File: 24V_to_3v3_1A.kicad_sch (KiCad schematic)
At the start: 6 parts, among them U2 R-78E3.3-1.0

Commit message: 24V updates
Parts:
- renumbered C12 to C3, C13 to C4, C14 to C5, C15 to C6, U2 to U1
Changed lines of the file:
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@@
   (symbol (lib_id "Regulator_Switching:R-78E3.3-1.0") (at 121.92 80.01 0) (unit 1)
     (in_bom yes) (on_board yes)
-    (property "Reference" "U2" (id 0) (at 121.92 73.8632 0))
+    (property "Reference" "U1" (id 0) (at 121.92 73.8632 0))
     (property "Value" "R-78E3.3-1.0" (id 1) (at 121.92 76.1746 0))
     (property "Footprint" "Converter_DCDC:Converter_DCDC_RECOM_R-78E-0.5_THT" (id 2) (at 123.19 86.36 0)
@@
   (symbol (lib_id "Device:C") (at 106.68 83.82 0) (unit 1)
     (in_bom yes) (on_board yes)
-    (property "Reference" "C13" (id 0) (at 109.601 82.6516 0)
+    (property "Reference" "C4" (id 0) (at 109.601 82.6516 0)
       (effects (font (size 1.27 1.27)) (justify left))
     )
@@
   (symbol (lib_id "Device:C") (at 96.52 83.82 0) (unit 1)
     (in_bom yes) (on_board yes)
-    (property "Reference" "C12" (id 0) (at 99.441 82.6516 0)
+    (property "Reference" "C3" (id 0) (at 99.441 82.6516 0)
       (effects (font (size 1.27 1.27)) (justify left))
     )
@@
   (symbol (lib_id "Device:C") (at 135.89 83.82 0) (unit 1)
     (in_bom yes) (on_board yes)
-    (property "Reference" "C14" (id 0) (at 138.811 82.6516 0)
+    (property "Reference" "C5" (id 0) (at 138.811 82.6516 0)
       (effects (font (size 1.27 1.27)) (justify left))
     )
@@
   (symbol (lib_id "Device:C") (at 148.59 83.82 0) (unit 1)
     (in_bom yes) (on_board yes)
-    (property "Reference" "C15" (id 0) (at 151.511 82.6516 0)
+    (property "Reference" "C6" (id 0) (at 151.511 82.6516 0)
       (effects (font (size 1.27 1.27)) (justify left))
     )
@@
   (symbol (lib_id "power:PWR_FLAG") (at 109.22 80.01 0) (unit 1)
     (in_bom yes) (on_board yes)
-    (property "Reference" "#FLG05" (id 0) (at 109.22 78.105 0)
+    (property "Reference" "#FLG04" (id 0) (at 109.22 78.105 0)
       (effects (font (size 1.27 1.27)) hide)
     )

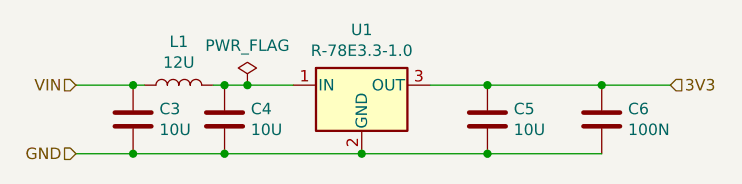
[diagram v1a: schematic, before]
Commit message: fix LT1161 symbol/sch
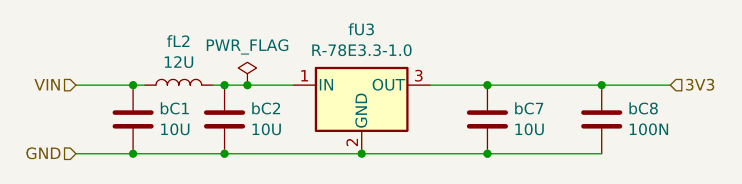
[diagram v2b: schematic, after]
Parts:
- renumbered C3 to bC1, C4 to bC2, C5 to bC7, C6 to bC8, L1 to fL2, U1 to fU3
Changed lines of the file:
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@@
   (symbol (lib_id "Regulator_Switching:R-78E3.3-1.0") (at 121.92 80.01 0) (unit 1)
     (in_bom yes) (on_board yes)
-    (property "Reference" "U1" (id 0) (at 121.92 73.8632 0))
+    (property "Reference" "fU3" (id 0) (at 121.92 73.8632 0))
     (property "Value" "R-78E3.3-1.0" (id 1) (at 121.92 76.1746 0))
     (property "Footprint" "Converter_DCDC:Converter_DCDC_RECOM_R-78E-0.5_THT" (id 2) (at 123.19 86.36 0)
@@
   (symbol (lib_id "Device:L") (at 101.6 80.01 90) (unit 1)
     (in_bom yes) (on_board yes)
-    (property "Reference" "L1" (id 0) (at 101.6 75.184 90))
+    (property "Reference" "fL2" (id 0) (at 101.6 75.184 90))
     (property "Value" "12U" (id 1) (at 101.6 77.4954 90))
     (property "Footprint" "Inductor_THT:L_Radial_D8.7mm_P5.00mm_Fastron_07HCP" (id 2) (at 101.6 80.01 0)
@@
   (symbol (lib_id "Device:C") (at 106.68 83.82 0) (unit 1)
     (in_bom yes) (on_board yes)
-    (property "Reference" "C4" (id 0) (at 109.601 82.6516 0)
+    (property "Reference" "bC2" (id 0) (at 109.601 82.6516 0)
       (effects (font (size 1.27 1.27)) (justify left))
     )
@@
   (symbol (lib_id "Device:C") (at 96.52 83.82 0) (unit 1)
     (in_bom yes) (on_board yes)
-    (property "Reference" "C3" (id 0) (at 99.441 82.6516 0)
+    (property "Reference" "bC1" (id 0) (at 99.441 82.6516 0)
       (effects (font (size 1.27 1.27)) (justify left))
     )
@@
   (symbol (lib_id "Device:C") (at 135.89 83.82 0) (unit 1)
     (in_bom yes) (on_board yes)
-    (property "Reference" "C5" (id 0) (at 138.811 82.6516 0)
+    (property "Reference" "bC7" (id 0) (at 138.811 82.6516 0)
       (effects (font (size 1.27 1.27)) (justify left))
     )
@@
   (symbol (lib_id "Device:C") (at 148.59 83.82 0) (unit 1)
     (in_bom yes) (on_board yes)
-    (property "Reference" "C6" (id 0) (at 151.511 82.6516 0)
+    (property "Reference" "bC8" (id 0) (at 151.511 82.6516 0)
       (effects (font (size 1.27 1.27)) (justify left))
     )
@@
   (symbol (lib_id "power:PWR_FLAG") (at 109.22 80.01 0) (unit 1)
     (in_bom yes) (on_board yes)
-    (property "Reference" "#FLG04" (id 0) (at 109.22 78.105 0)
+    (property "Reference" "#FLG03" (id 0) (at 109.22 78.105 0)
       (effects (font (size 1.27 1.27)) hide)
     )
